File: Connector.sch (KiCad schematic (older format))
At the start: 9 parts, among them J6 TE_Eurocard_96pole, J9 Conn_01x02, U8 74AHC244, U9 74AHC244

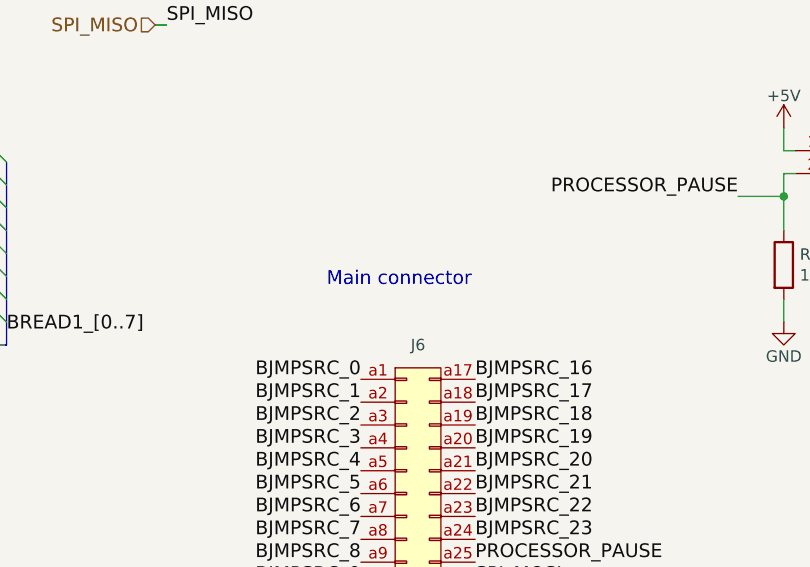
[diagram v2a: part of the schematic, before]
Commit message: Multiple change : Replacing old custom "LTC6994-1" symbol with the Kicad symbol "LTC6994xS6-1" Replacing old custom "LM810" symbol with the Kicad symbol "LM810" Replacing all hidden power pins symbols (hidden pins bug) Renaming "Main connector" to "SPS1 Processor connector" Removing old symbols, cleaning Replacing symbol "CD74AC238" with a new one
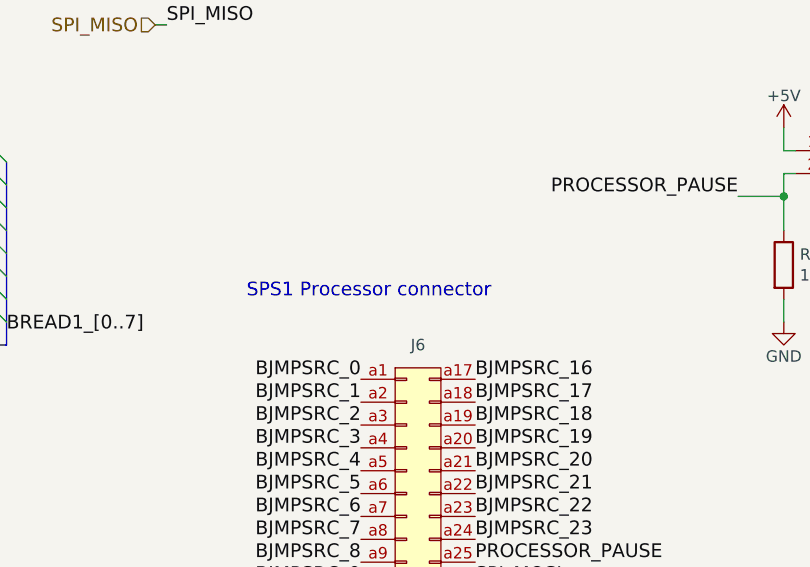
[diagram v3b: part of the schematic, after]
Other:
- note added: "SPS1 Processor connector"
- note removed: "Main connector"
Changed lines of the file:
@@
 Comment4 ""
 $EndDescr
-Text Notes 4600 1900 0    60   ~ 0
-Main connector
+Text Notes 4250 1950 0    60   ~ 0
+SPS1 Processor connector
 Text Label 8300 1800 0    60   ~ 0
 NUMBER_0
